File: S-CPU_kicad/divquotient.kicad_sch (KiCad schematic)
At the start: 97 parts

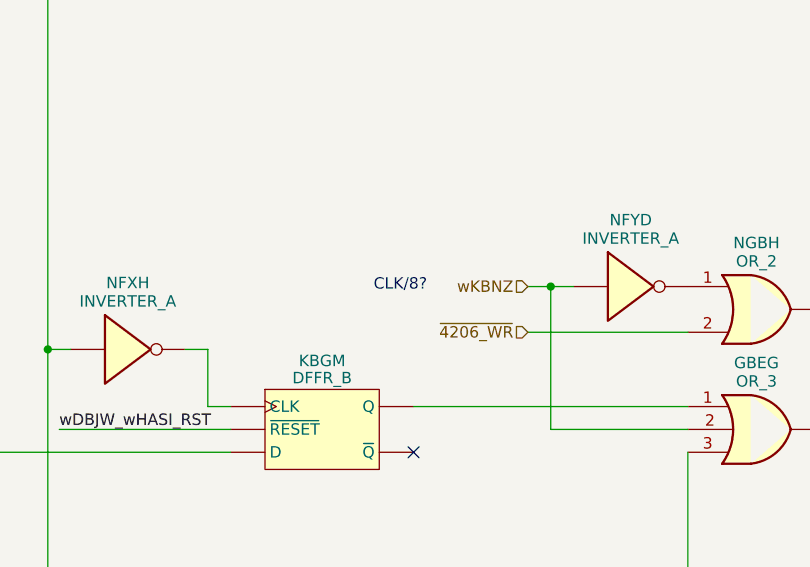
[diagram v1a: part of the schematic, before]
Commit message: ADDR and DAT bus progress
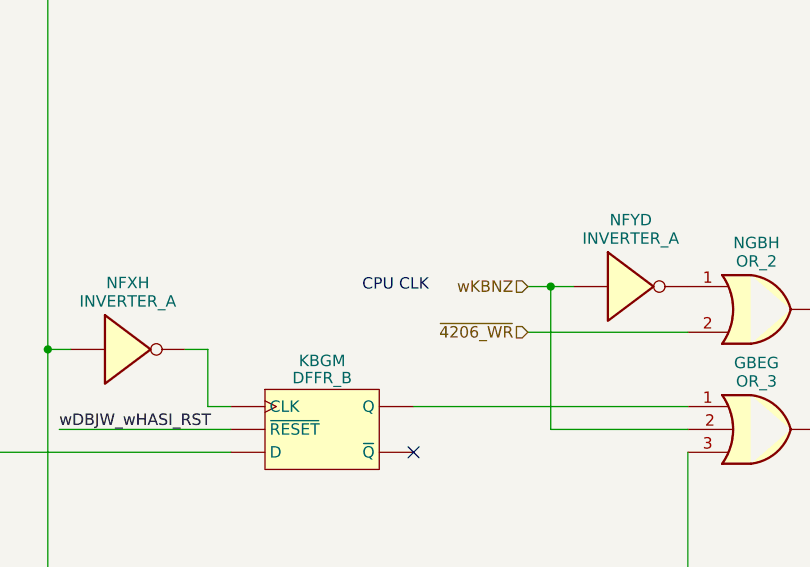
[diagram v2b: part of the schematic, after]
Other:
- note added: "CPU CLK"
- note removed: "CLK/8?"
- company: (none) -> Regis Galland
- title: (none) -> SNES S-CPU Schematics 
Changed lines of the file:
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@@
 (kicad_sch (version 20230121) (generator eeschema)
   (paper "A1")
+  (title_block
+    (title "SNES S-CPU Schematics ")
+    (date "2023-06-14")
+    (rev "0.1")
+    (company "Regis Galland")
+  )
   (junction (at 346.71 195.58) (diameter 0) (color 0 0 0 0)
   )
@@
     (effects (font (size 5 5) (thickness 1) bold) (justify left bottom))
   )
-  (text "CLK/8?\n" (at 605.155 518.795 0)
+  (text "CPU CLK" (at 603.885 518.795 0)
     (effects (font (size 1.27 1.27)) (justify left bottom))
   )

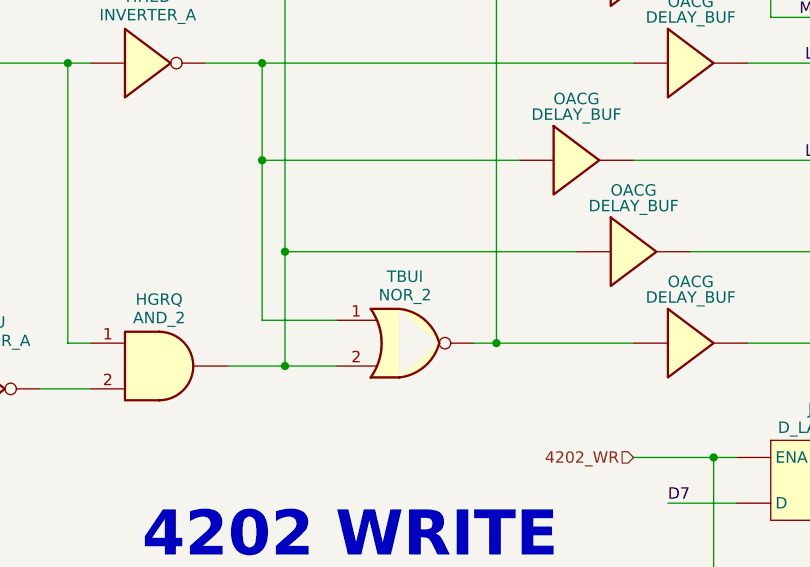
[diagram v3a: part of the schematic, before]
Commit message: Some cells had the wrong ID in the producter remainder sheet. Allocation of new names in spreadsheet for cells in the DMA section
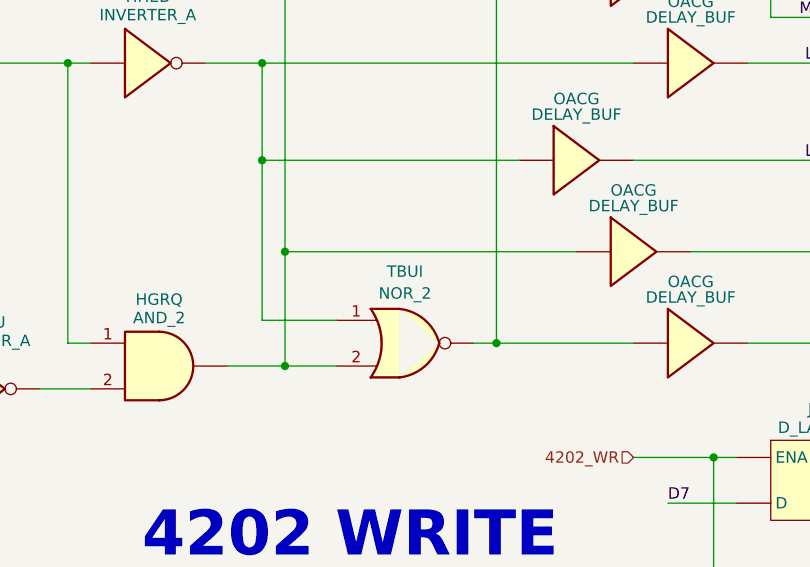
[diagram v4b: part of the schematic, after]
